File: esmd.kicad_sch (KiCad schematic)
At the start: 8 parts, among them J1 Conn_01x04, J2 Conn_01x08, J3 Conn_01x02, J4 Conn_01x02, U2 LM78M05_TO252, U3 74HC245

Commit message: Make it triple.
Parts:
- removed J4: Conn_01x02, Connector_PinSocket_2.54mm:PinSocket_1x02_P2.54mm_Vertical, symbol Connector_Generic:Conn_01x02
- added C2, C3: 100n, Capacitor_SMD:C_0603_1608Metric, symbol Device:C
- added H1, H2: MountingHole, MountingHole:MountingHole_3.2mm_M3, symbol Mechanical:MountingHole
- added J3, J5: Conn_01x04, Connector_JST:JST_XH_B4B-XH-A_1x04_P2.50mm_Vertical, symbol Connector_Generic:Conn_01x04
- added J4, J6: Conn_01x08, Connector_JST:JST_XH_B6B-XH-A_1x06_P2.50mm_Vertical, symbol Connector_Generic:Conn_01x06
- added R2, R3: 1k, Resistor_SMD:R_0603_1608Metric, symbol Device:R
- added U1, U4: 74HC245, Package_SO:SSOP-20_5.3x7.2mm_P0.65mm, symbol 74xx:74HC245
- J1: footprint Connector_JST:JST_XH_S4B-XH-A_1x04_P2.50mm_Horizontal -> Connector_JST:JST_XH_B4B-XH-A_1x04_P2.50mm_Vertical
- J2: footprint Connector_JST:JST_XH_S6B-XH-A_1x06_P2.50mm_Horizontal -> Connector_JST:JST_XH_B6B-XH-A_1x06_P2.50mm_Vertical
- renumbered J3 to J7
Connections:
- net +5V: now also C2.1, C3.1, R2.1, R3.1, U1.20 (VCC), U4.20 (VCC)
- net GND: now also C2.2, C3.2, J3.4 (Pin_4), J4.2 (Pin_2), J4.4 (Pin_4), J4.6 (Pin_6), J5.4 (Pin_4), J6.2 (Pin_2), J6.4 (Pin_4), J6.6 (Pin_6), U1.10 (GND), U1.19 (CE), U4.10 (GND), U4.19 (CE)
- net Dir renamed Dir1
- net Dir_out renamed Dir_out1
- net Enable renamed Enable1
- net Enable_out renamed Enable_out1
- net Step renamed Step1
- net Step_out renamed Step_out1
- new net: R2.2, U1.1 (A->B), U1.2 (A0), U1.4 (A2), U1.6 (A4), U1.8 (A6), U1.9 (A7)
- new net: R3.2, U4.1 (A->B), U4.2 (A0), U4.4 (A2), U4.6 (A4), U4.8 (A6), U4.9 (A7)
- new net Dir2: J3.3 (Pin_3), U1.7 (A5)
- new net Dir3: J5.3 (Pin_3), U4.7 (A5)
- new net Dir_out2: J4.1 (Pin_1), U1.13 (B5)
- new net Dir_out3: J6.1 (Pin_1), U4.13 (B5)
- new net Enable2: J3.1 (Pin_1), U1.3 (A1)
- new net Enable3: J5.1 (Pin_1), U4.3 (A1)
- new net Enable_out2: J4.5 (Pin_5), U1.17 (B1)
- new net Enable_out3: J6.5 (Pin_5), U4.17 (B1)
- new net Step2: J3.2 (Pin_2), U1.5 (A3)
- new net Step3: J5.2 (Pin_2), U4.5 (A3)
- new net Step_out2: J4.3 (Pin_3), U1.15 (B3)
- new net Step_out3: J6.3 (Pin_3), U4.15 (B3)
- no-connect marks 5 -> 15
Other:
- moved on the sheet: C1, J1, J2, J7, R1, U2, U3

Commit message: Fix footprints.
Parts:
- U1, U3, U4: footprint Package_SO:SSOP-20_5.3x7.2mm_P0.65mm -> Package_SO:SOP-20_7.5x12.8mm_P1.27mm
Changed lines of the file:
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@@
       (effects (font (size 1.27 1.27)) (justify left))
     )
-    (property "Footprint" "Package_SO:SSOP-20_5.3x7.2mm_P0.65mm" (at 55.88 127 0)
+    (property "Footprint" "Package_SO:SOP-20_7.5x12.8mm_P1.27mm" (at 55.88 127 0)
       (effects (font (size 1.27 1.27)) hide)
     )
@@
       (effects (font (size 1.27 1.27)) (justify left))
     )
-    (property "Footprint" "Package_SO:SSOP-20_5.3x7.2mm_P0.65mm" (at 210.82 127 0)
+    (property "Footprint" "Package_SO:SOP-20_7.5x12.8mm_P1.27mm" (at 210.82 127 0)
       (effects (font (size 1.27 1.27)) hide)
     )
@@
       (effects (font (size 1.27 1.27)) (justify left))
     )
-    (property "Footprint" "Package_SO:SSOP-20_5.3x7.2mm_P0.65mm" (at 132.08 127 0)
-      (effects (font (size 1.27 1.27)) hide)
-    )
+    (property "Footprint" "Package_SO:SOP-20_7.5x12.8mm_P1.27mm" (at 132.08 127 0)
+      (effects (font (size 1.27 1.27)) hide)
+    )

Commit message: Route.
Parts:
- U1, U3, U4: footprint Package_SO:SOP-20_7.5x12.8mm_P1.27mm -> Package_SO:SO-20_5.3x12.6mm_P1.27mm
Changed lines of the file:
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@@
       (effects (font (size 1.27 1.27)) (justify left))
     )
-    (property "Footprint" "Package_SO:SOP-20_7.5x12.8mm_P1.27mm" (at 55.88 127 0)
+    (property "Footprint" "Package_SO:SO-20_5.3x12.6mm_P1.27mm" (at 55.88 127 0)
       (effects (font (size 1.27 1.27)) hide)
     )
@@
       (effects (font (size 1.27 1.27)) (justify left))
     )
-    (property "Footprint" "Package_SO:SOP-20_7.5x12.8mm_P1.27mm" (at 210.82 127 0)
+    (property "Footprint" "Package_SO:SO-20_5.3x12.6mm_P1.27mm" (at 210.82 127 0)
       (effects (font (size 1.27 1.27)) hide)
     )
@@
       (effects (font (size 1.27 1.27)) (justify left))
     )
-    (property "Footprint" "Package_SO:SOP-20_7.5x12.8mm_P1.27mm" (at 132.08 127 0)
-      (effects (font (size 1.27 1.27)) hide)
-    )
+    (property "Footprint" "Package_SO:SO-20_5.3x12.6mm_P1.27mm" (at 132.08 127 0)
+      (effects (font (size 1.27 1.27)) hide)
+    )

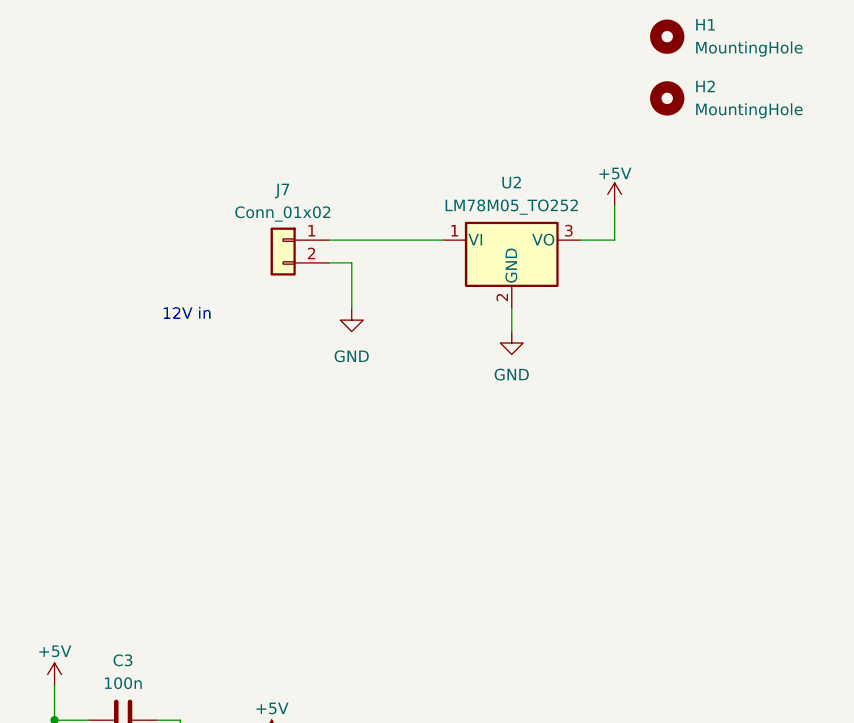
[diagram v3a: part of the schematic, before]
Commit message: Add support for 5V supply.
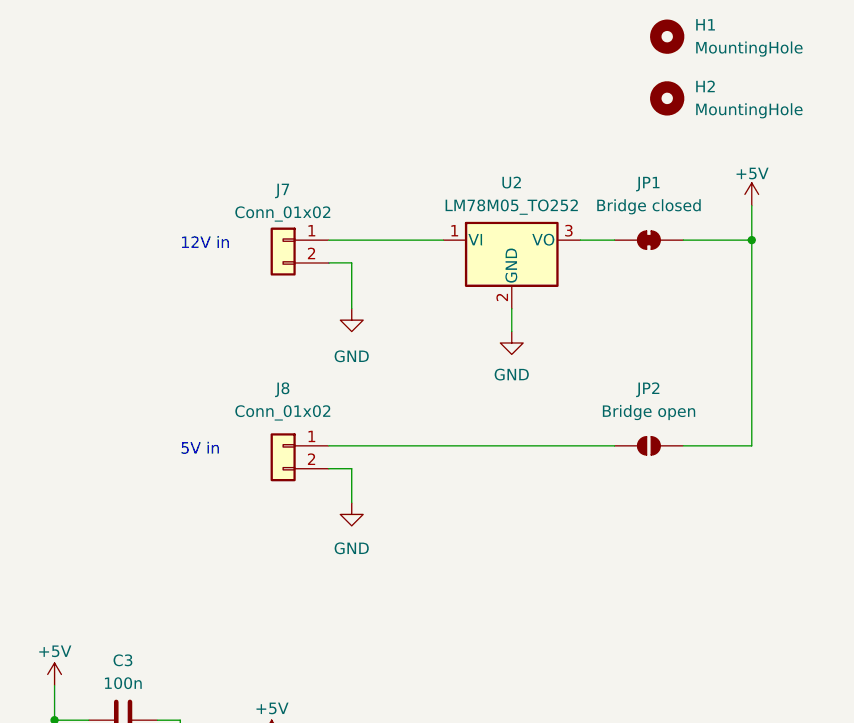
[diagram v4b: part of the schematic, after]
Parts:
- added J8: Conn_01x02, Connector_JST:JST_XH_B2B-XH-A_1x02_P2.50mm_Vertical, symbol Connector_Generic:Conn_01x02
- added JP1: Bridge closed, Jumper:SolderJumper-2_P1.3mm_Bridged_RoundedPad1.0x1.5mm, symbol Jumper:SolderJumper_2_Bridged
- added JP2: Bridge open, Jumper:SolderJumper-2_P1.3mm_Open_RoundedPad1.0x1.5mm, symbol Jumper:SolderJumper_2_Open
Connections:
- net +5V: now also JP1.1 (A), JP2.2 (B); no longer U2.3 (VO)
- net GND: now also J8.2 (Pin_2)
- new net: JP1.2 (B), U2.3 (VO)
- new net: J8.1 (Pin_1), JP2.1 (A)
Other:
- note added: "5V in"

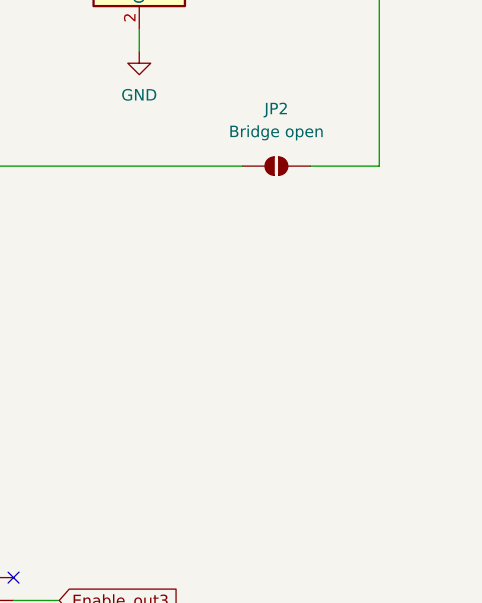
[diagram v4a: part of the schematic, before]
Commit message: Add power LED.
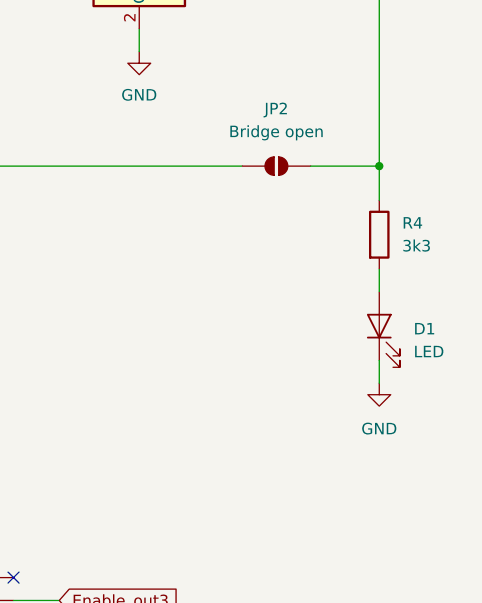
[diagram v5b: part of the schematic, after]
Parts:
- added D1: LED, PCM_LED_SMD_AKL:LED_0603_1608Metric, symbol Device:LED
- added R4: 3k3, PCM_Resistor_SMD_AKL:R_0603_1608Metric, symbol Device:R
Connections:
- net +5V: now also R4.1
- net GND: now also D1.1 (K)
- new net: D1.2 (A), R4.2
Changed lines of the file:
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@@
 	)
 	(junction
+		(at 264.16 68.58)
+		(diameter 0)
+		(color 0 0 0 0)
+	)
+	(junction
 		(at 107.95 114.3)
 		(diameter 0)
@@
 	(wire
 		(pts
+			(xy 264.16 68.58) (xy 264.16 72.39)
+		)
+		(stroke
+			(width 0)
+			(type default)
+		)
+	)
+	(wire
+		(pts
 			(xy 107.95 129.54) (xy 107.95 132.08)
 		)
@@
 	(wire
 		(pts
+			(xy 264.16 80.01) (xy 264.16 82.55)
+		)
+		(stroke
+			(width 0)
+			(type default)
+		)
+	)
+	(wire
+		(pts
 			(xy 74.93 26.67) (xy 80.01 26.67)
 		)
@@
 	(wire
 		(pts
+			(xy 264.16 90.17) (xy 264.16 92.71)
+		)
+		(stroke
+			(width 0)
+			(type default)
+		)
+	)
+	(wire
+		(pts
 			(xy 82.55 54.61) (xy 80.01 54.61)
 		)
@@
 	)
 	(symbol
+		(lib_id "Device:LED")
+		(at 264.16 86.36 90)
+		(unit 1)
+		(exclude_from_sim no)
+		(in_bom yes)
+		(on_board yes)
+		(dnp no)
+		(fields_autoplaced yes)
+		(property "Reference" "D1"
+			(at 267.97 86.6901 90)
+			(effects
+				(font
+					(size 1.27 1.27)
+				)
+				(justify right)
+			)
+		)
+		(property "Value" "LED"
+			(at 267.97 89.2301 90)
+			(effects
+				(font
+					(size 1.27 1.27)
+				)
+				(justify right)
+			)
+		)
+		(property "Footprint" "PCM_LED_SMD_AKL:LED_0603_1608Metric"
+			(at 264.16 86.36 0)
+			(effects
+				(font
+					(size 1.27 1.27)
+				)
+				(hide yes)
+			)
+		)
+		(property "Datasheet" "~"
+			(at 264.16 86.36 0)
+			(effects
+				(font
+					(size 1.27 1.27)
+				)
+				(hide yes)
+			)
+		)
+		(property "Description" "Light emitting diode"
+			(at 264.16 86.36 0)
+			(effects
+				(font
+					(size 1.27 1.27)
+				)
+				(hide yes)
+			)
+		)
+		(pin "1"
+		)
+		(pin "2"
+		)
+		(instances
+			(project ""
+				(path "/5e0cb9fd-a755-4107-9e53-712af8b2f94c"
+					(reference "D1")
+					(unit 1)
+				)
+			)
+		)
+	)
+	(symbol
+		(lib_id "power:GND")
+		(at 264.16 92.71 0)
+		(unit 1)
+		(exclude_from_sim no)
+		(in_bom yes)
+		(on_board yes)
+		(dnp no)
+		(fields_autoplaced yes)
+		(property "Reference" "#PWR023"
+			(at 264.16 99.06 0)
+			(effects
+				(font
+					(size 1.27 1.27)
+				)
+				(hide yes)
+			)
+		)
+		(property "Value" "GND"
+			(at 264.16 97.79 0)
+			(effects
+				(font
+					(size 1.27 1.27)
+				)
+			)
+		)
+		(property "Footprint" ""
+			(at 264.16 92.71 0)
+			(effects
+				(font
+					(size 1.27 1.27)
+				)
+				(hide yes)
+			)
+		)
+		(property "Datasheet" ""
+			(at 264.16 92.71 0)
+			(effects
+				(font
+					(size 1.27 1.27)
+				)
+				(hide yes)
+			)
+		)
+		(property "Description" "Power flag, ground"
+			(at 264.16 92.71 0)
+			(effects
+				(font
+					(size 1.27 1.27)
+				)
+				(hide yes)
+			)
+		)
+		(pin "1"
+		)
+		(instances
+			(project ""
+				(path "/5e0cb9fd-a755-4107-9e53-712af8b2f94c"
+					(reference "#PWR023")
+					(unit 1)
+				)
+			)
+		)
+	)
+	(symbol
 		(lib_id "power:GND")
 		(at 219.71 74.93 0)
@@
 					(unit 1)
 				)
+			)
+		)
+	)
+	(symbol
+		(lib_id "Device:R")
+		(at 264.16 76.2 0)
+		(unit 1)
+		(exclude_from_sim no)
+		(in_bom yes)
+		(on_board yes)
+		(dnp no)
+		(fields_autoplaced yes)
+		(property "Reference" "R4"
+			(at 266.7 74.9299 0)
+			(effects
+				(font
+					(size 1.27 1.27)
+				)
+				(justify left)
+			)
+		)
+		(property "Value" "3k3"
+			(at 266.7 77.4699 0)
+			(effects
+				(font
+					(size 1.27 1.27)
+				)
+				(justify left)
+			)
+		)
+		(property "Footprint" "PCM_Resistor_SMD_AKL:R_0603_1608Metric"
+			(at 262.382 76.2 90)
+			(effects
+				(font
+					(size 1.27 1.27)
+				)
+				(hide yes)
+			)
+		)
+		(property "Datasheet" "~"
+			(at 264.16 76.2 0)
+			(effects
+				(font
+					(size 1.27 1.27)
+				)
+				(hide yes)
+			)
+		)
+		(property "Description" "Resistor"
+			(at 264.16 76.2 0)
+			(effects
+				(font
+					(size 1.27 1.27)
+				)
+				(hide yes)
+			)
+		)
+		(pin "1"
+		)
+		(pin "2"
+		)
+		(instances
+			(project ""
+				(path "/5e0cb9fd-a755-4107-9e53-712af8b2f94c"
+					(reference "R4")
+					(unit 1)
+				)

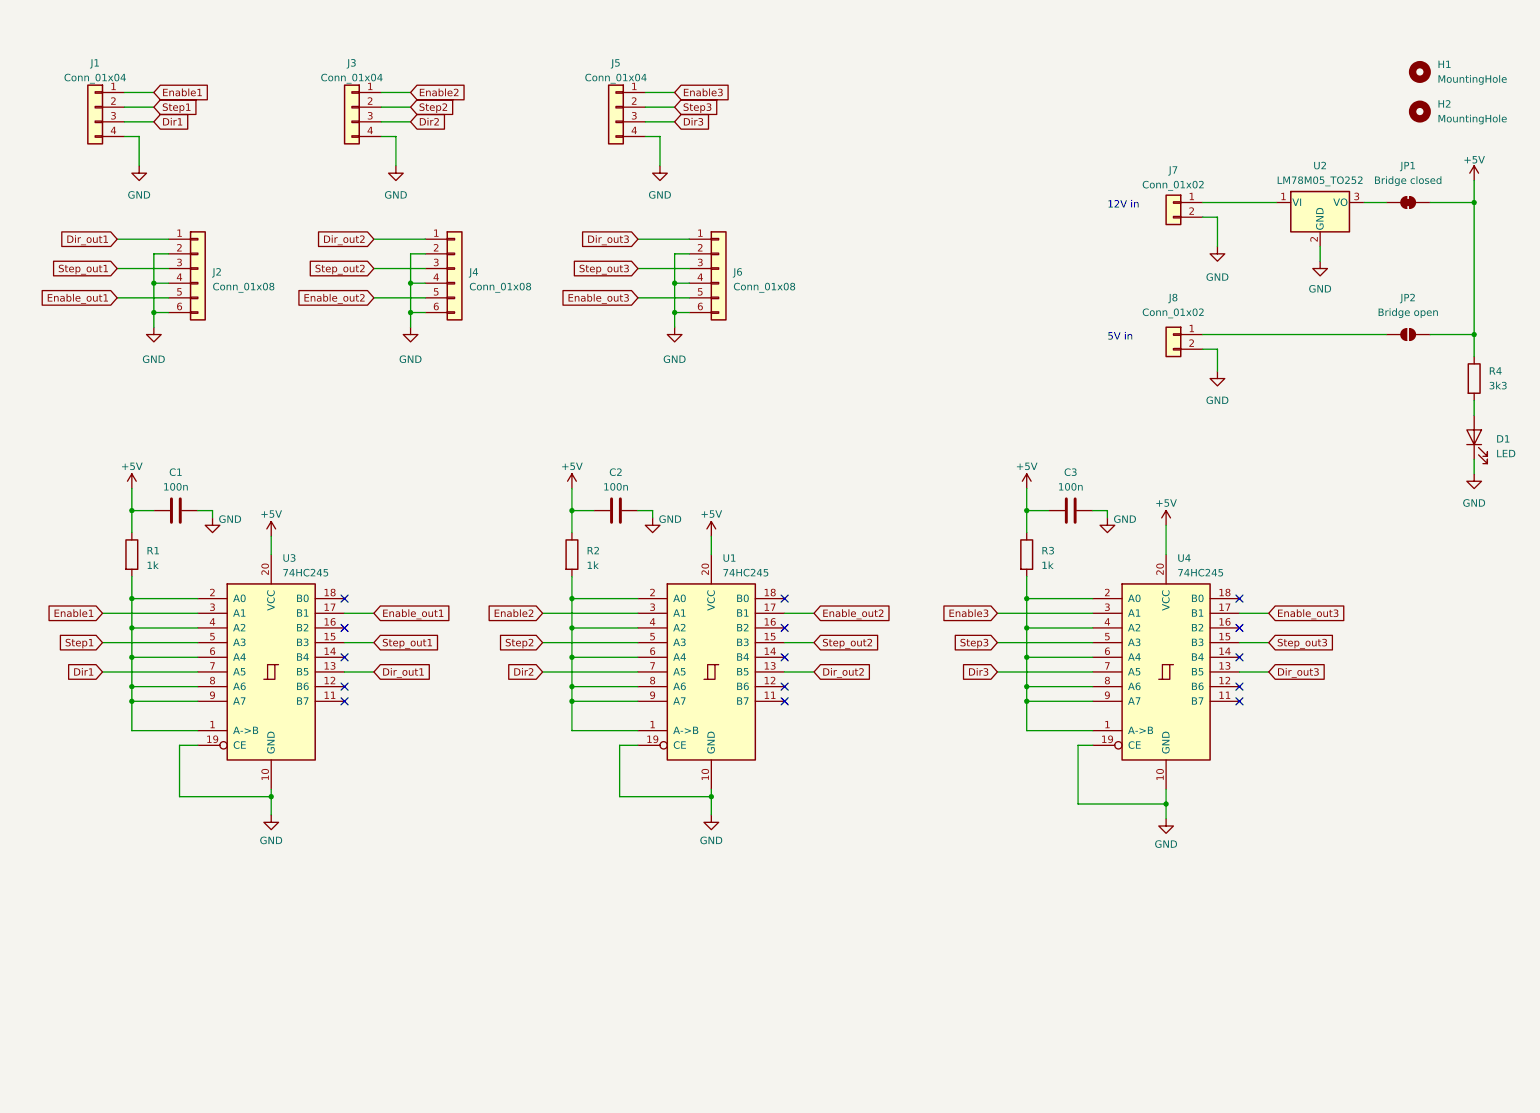
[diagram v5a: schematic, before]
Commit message: Use only two drivers.
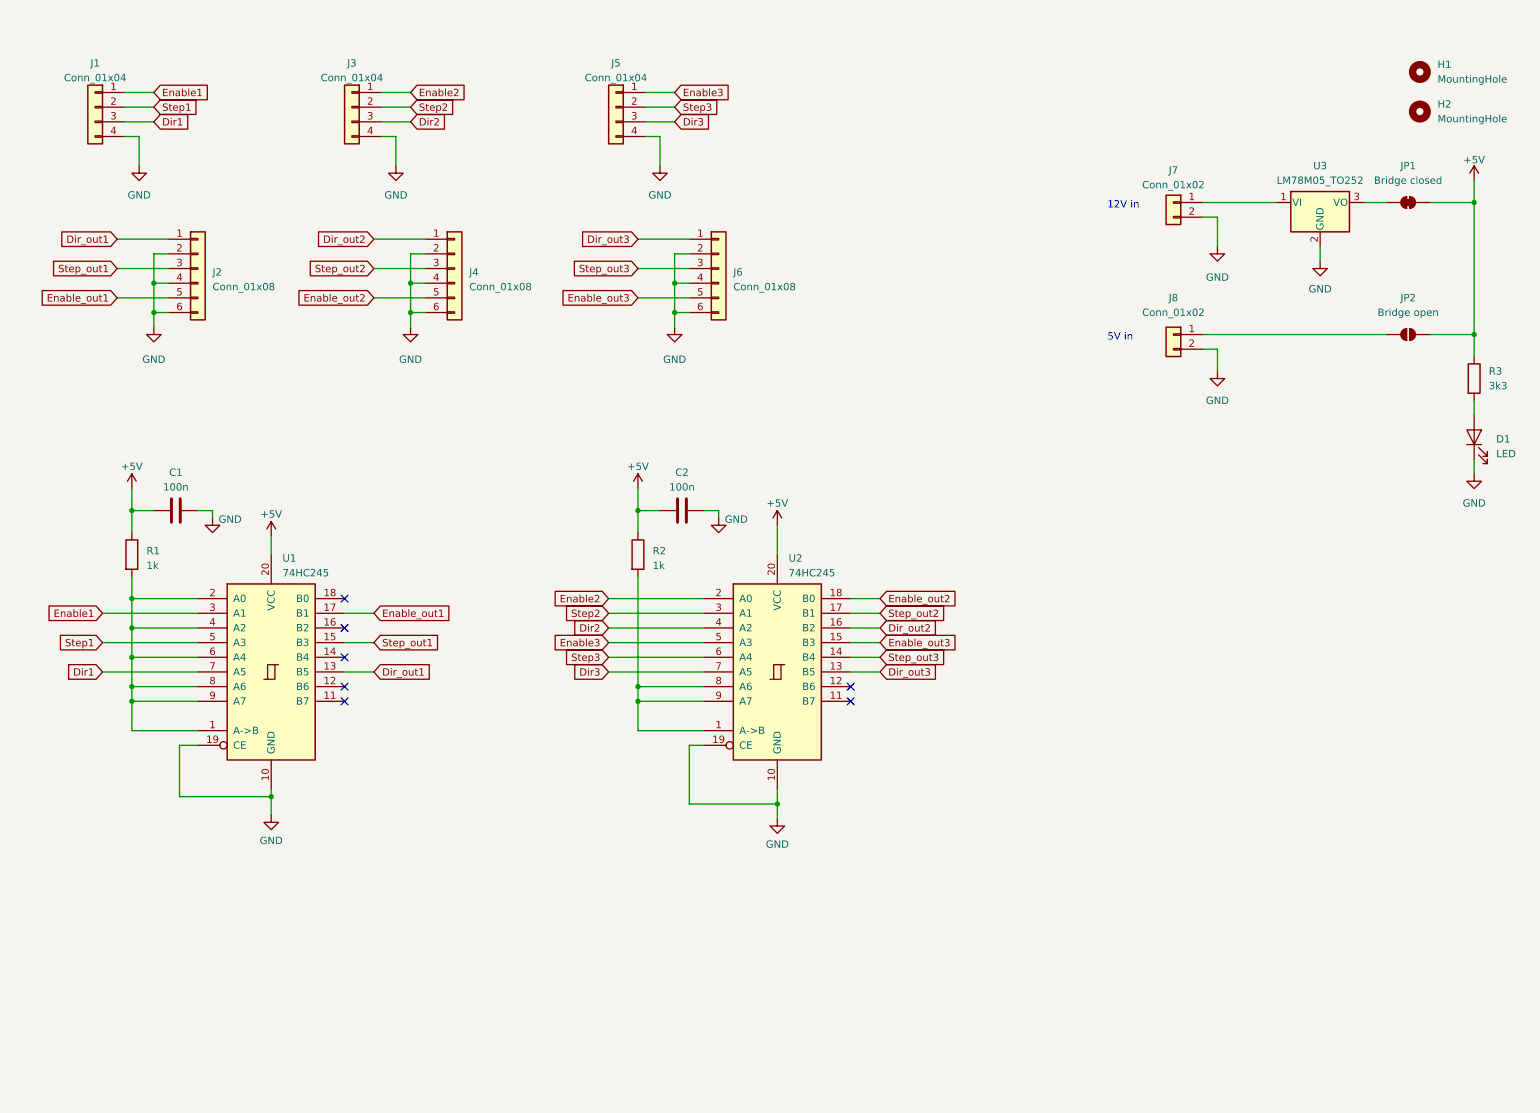
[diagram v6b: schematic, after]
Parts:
- removed C2: 100n, Capacitor_SMD:C_0603_1608Metric, symbol Device:C
- removed R2: 1k, Resistor_SMD:R_0603_1608Metric, symbol Device:R
- removed U1: 74HC245, Package_SO:SO-20_5.3x12.6mm_P1.27mm, symbol 74xx:74HC245
- renumbered C3 to C2, R3 to R2, R4 to R3, U3 to U1, U4 to U2, U2 to U3
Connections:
- net Dir2: now also U2.4 (A2)
- net Dir_out2: now also U2.16 (B2)
- net Enable2: now also U2.2 (A0)
- net Enable3: now also U2.5 (A3); no longer U2.3 (A1)
- net Enable_out2: now also U2.18 (B0)
- net Enable_out3: now also U2.15 (B3); no longer U2.17 (B1)
- net Step2: now also U2.3 (A1)
- net Step3: now also U2.6 (A4); no longer U2.5 (A3)
- net Step_out2: now also U2.17 (B1)
- net Step_out3: now also U2.14 (B4); no longer U2.15 (B3)
- net at R2.2, U2.1 (A->B), U2.8 (A6)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: no longer U2.2 (A0), U2.4 (A2), U2.6 (A4)
- no-connect marks 15 -> 7
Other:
- moved on the sheet: C2, R2, U2
